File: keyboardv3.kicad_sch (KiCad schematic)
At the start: 171 parts, among them U1 Pico

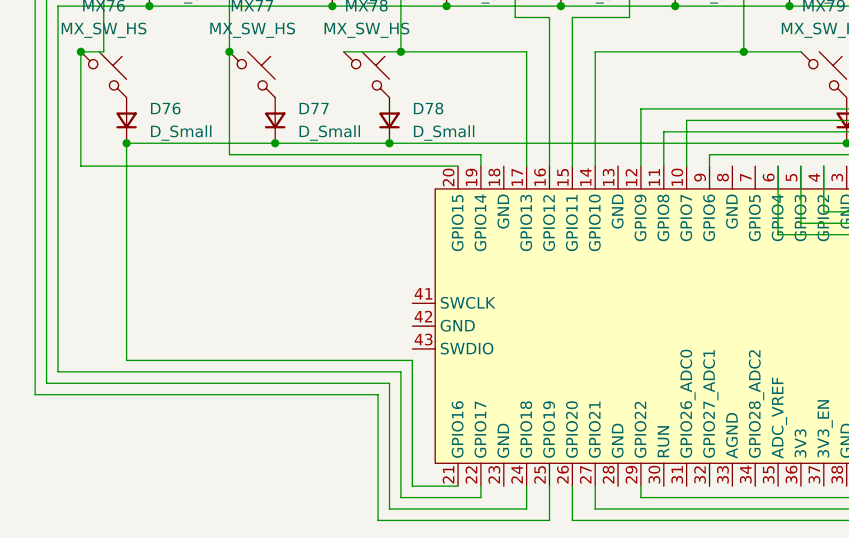
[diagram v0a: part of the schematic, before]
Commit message: Tweaked initial full keyboard design diodes
Switched from 0805 smd diodes to DO-35 through-hole diodes to allow for easier assembly
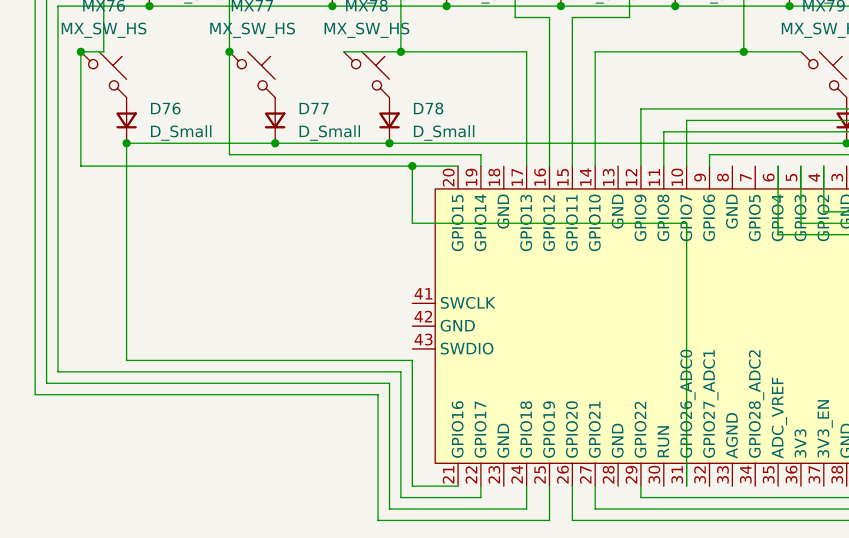
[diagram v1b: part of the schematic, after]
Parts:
- D1, D10, D11, D12, D13, D14, D15, D16, D17, D18, D19, D2, D20, D21, D22, D23, D24, D25, D26, D27, D28, D29, D3, D30, D31, D32, D33, D34, D35, D36, D37, D38, D39, D4, D40, D41, D42, D43, D44, D45, D46, D47, D48, D49, D5, D50, D51, D52, D53, D54, D55, D56, D57, D58, D59, D6, D60, D61, D62, D63, D64, D65, D66, D67, D68, D69, D7, D70, D71, D72, D73, D74, D75, D76, D77, D78, D79, D8, D80, D81, D82, D83, D84, D85, D9: footprint Diode_SMD:D_0805_2012Metric_Pad1.15x1.40mm_HandSolder -> Diode_THT:D_DO-35_SOD27_P7.62mm_Horizontal
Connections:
- net at MX18.1, MX33.1, MX4.1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: now also U1.31 (GPIO26_ADC0)
